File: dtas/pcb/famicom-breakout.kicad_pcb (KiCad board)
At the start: 2 copper layers, 88.5 x 57.4 mm, 23 parts

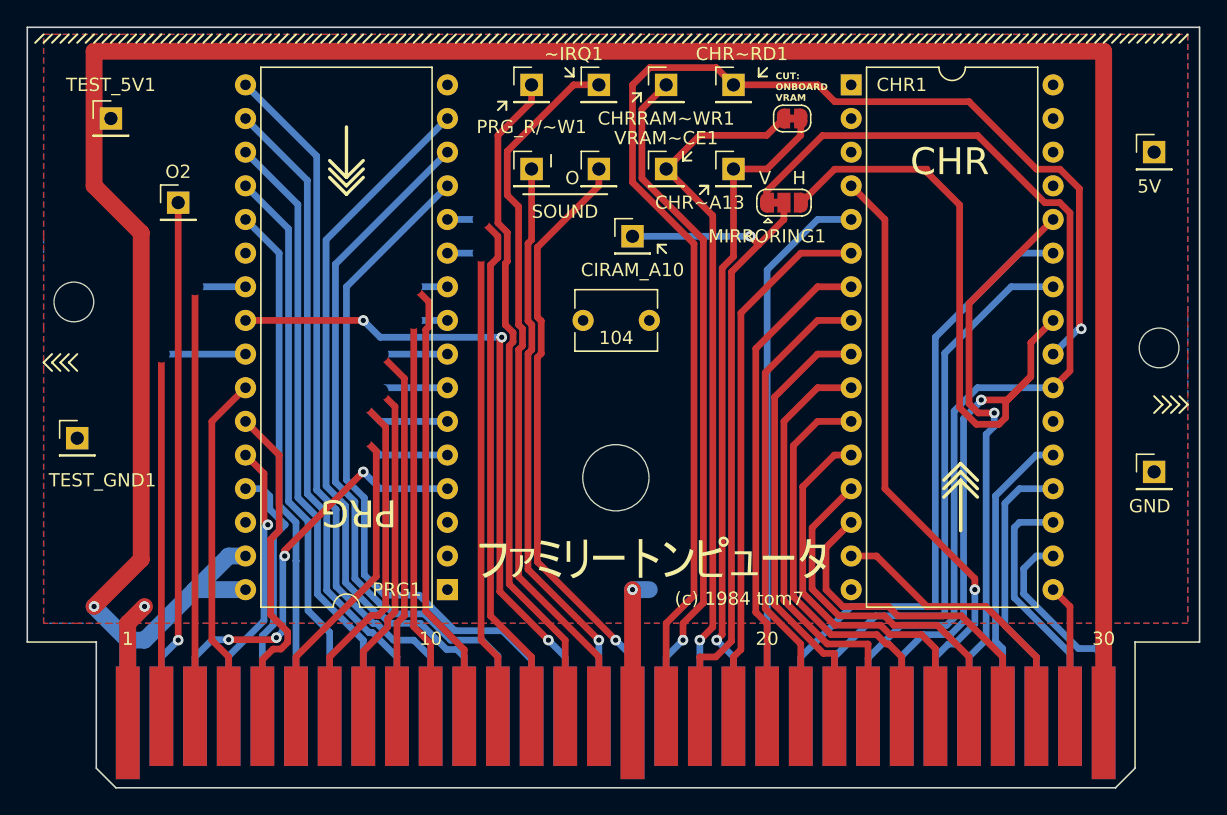
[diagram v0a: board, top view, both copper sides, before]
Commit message: Version 2 of board, which just adds many additional test points and jumpers so I can debug the thing
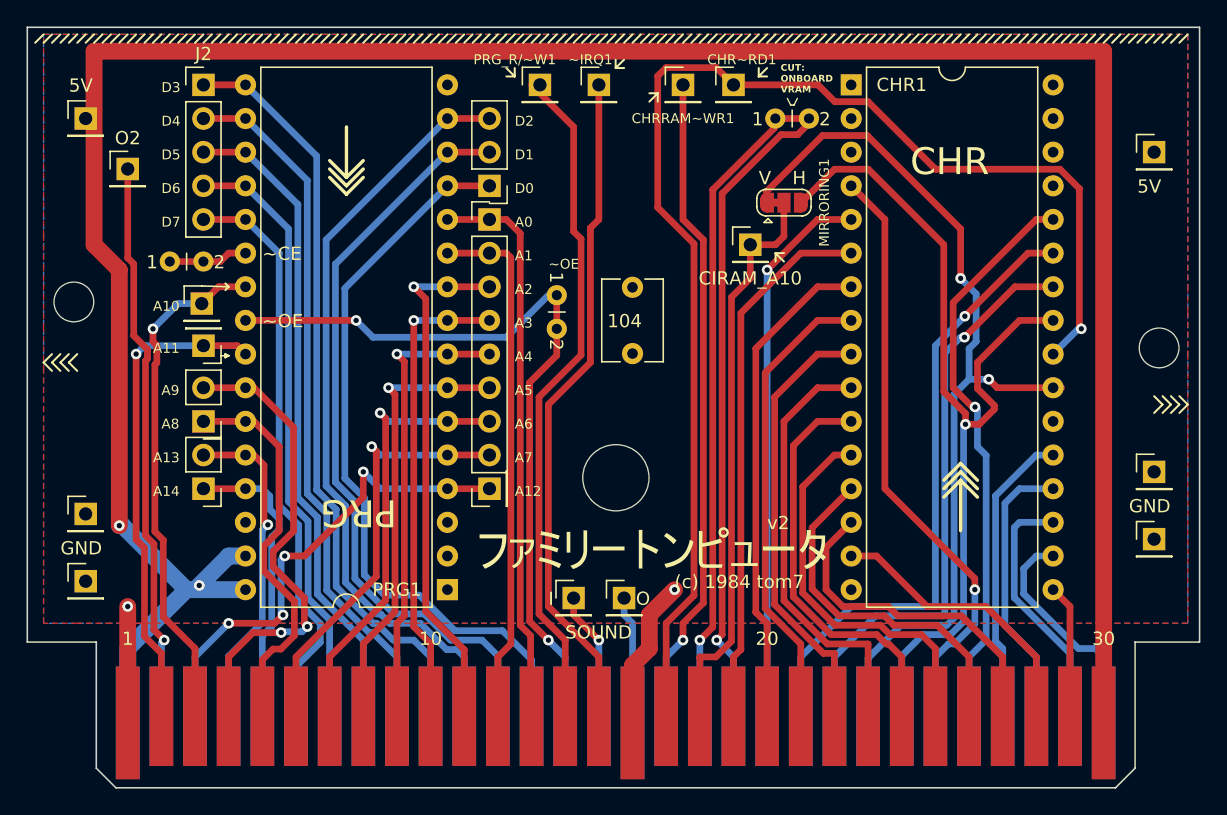
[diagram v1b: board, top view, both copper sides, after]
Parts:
- removed CHR~A13, VRAM~CE1: Conn_01x01, Connector_PinHeader_2.54mm:PinHeader_1x01_P2.54mm_Vertical
- added A10: PRG_ADDR_A10, Connector_PinHeader_2.54mm:PinHeader_1x01_P2.54mm_Vertical, F.Cu at (42.4, 52.1)
- added A11: PRG_ADDR_A11, Connector_PinHeader_2.54mm:PinHeader_1x01_P2.54mm_Vertical, F.Cu at (42.5, 55.2)
- added A12: PRG_ADDR_A12, Connector_PinHeader_2.54mm:PinHeader_1x01_P2.54mm_Vertical, F.Cu at (64.1, 66.0)
- added J1: PRG_DATA0_2, Connector_PinHeader_2.54mm:PinHeader_1x03_P2.54mm_Vertical, F.Cu at (64.1, 43.2)
- added J2: PRG_DATA3_7, Connector_PinHeader_2.54mm:PinHeader_1x05_P2.54mm_Vertical, F.Cu at (42.5, 35.6)
- added J3: PRG_ADDR_0_7, Connector_PinHeader_2.54mm:PinHeader_1x08_P2.54mm_Vertical, F.Cu at (64.1, 45.7)
- added J4: PRG_ADDR_8_9, Connector_PinHeader_2.54mm:PinHeader_1x02_P2.54mm_Vertical, F.Cu at (42.5, 61.0)
- added J5: PRG_ADDR_13_14, Connector_PinHeader_2.54mm:PinHeader_1x02_P2.54mm_Vertical, F.Cu at (42.5, 66.0)
- added JP2: PRG_OE_44, famicom:testjumperclosed, F.Cu at (69.2, 52.7)
- added JP3: PRG_CE_GND, famicom:testjumperclosed, F.Cu at (41.3, 48.9)
- added TEST_GND3: Conn_01x01, Connector_PinHeader_2.54mm:PinHeader_1x01_P2.54mm_Vertical, F.Cu at (33.7, 73.0)
- added TEST_GND4: Conn_01x01, Connector_PinHeader_2.54mm:PinHeader_1x01_P2.54mm_Vertical, F.Cu at (114.3, 69.8)
- JP1: footprint Jumper:SolderJumper-2_P1.3mm_Bridged_RoundedPad1.0x1.5mm -> famicom:testjumperclosed
- moved SOUND_I1 32.5 mm to (70.5, 74.3)
- moved SOUND_O1 32.4 mm to (74.3, 74.3)
- moved CIRAM_A10 8.91 mm to (83.8, 47.6)
- moved TEST_GND1 5.75 mm to (33.7, 67.9)
- moved O2 4.58 mm to (36.8, 41.9)
- moved C1 4.49 mm to (74.9, 55.8), turned to 90 degrees
- moved TEST_5V1 1.91 mm to (33.7, 38.1)
- moved CHRRAM~WR1 1.27 mm to (78.7, 35.6)
- moved PRG_R/~W1 0.63 mm to (67.9, 35.6)
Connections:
- PRG1 pad 22: GND -> Net-(JP3-B)
- PRG1 pad 24: Net-(EDGE1-PRG_ROM_~CE) -> Net-(JP2-A)
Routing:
- net Net-(EDGE1-SOUND_O): track 46.9 -> 9.68 mm, vias 1 -> 0
- net Net-(EDGE1-SOUND_I): track 43.9 -> 9.71 mm
- net Net-(JP2-A): track 0.00 -> 24.7 mm, vias 0 -> 1
- net Net-(EDGE1-PRG_ROM_~CE): track 50.6 -> 31.1 mm, vias 3 -> 1
- net Net-(EDGE1-PRG_A09): track 26.4 -> 36.1 mm, vias 0 -> 2
- net Net-(CIRAM_A10-Pin_1): track 51.9 -> 43.2 mm, vias 1 -> 0
- net Net-(CHR1-A10): track 77.6 -> 70.1 mm, vias 0 -> 2
- net Net-(CHR1-A11): track 74.6 -> 67.4 mm
- net Net-(EDGE1-VRAM_~CE): track 53.6 -> 47.4 mm
- net 5v: track 196.9 -> 191.8 mm, vias 1 -> 2
- net Net-(EDGE1-PRG_D7): track 39.1 -> 43.8 mm
- net Net-(EDGE1-PRG_A08): track 25.2 -> 29.6 mm
- net Net-(EDGE1-~IRQ): track 54.7 -> 50.8 mm
- net Net-(EDGE1-PRG_A13): track 21.6 -> 25.2 mm
- net Net-(A12-Pin_1): track 33.3 -> 36.8 mm
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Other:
- board text added: "A0"
- board text added: "A1"
- board text added: "A10"
- board text added: "A11"
- board text added: "A12"
- board text added: "A13"
- board text added: "A14"
- board text added: "A2"
- board text added: "A3"
- board text added: "A4"
- board text added: "A5"
- board text added: "A6"
- board text added: "A7"
- board text added: "A8"
- board text added: "A9"
- board text added: "D0"
- board text added: "D1"
- board text added: "D2"
- board text added: "D3"
- board text added: "D4"
- board text added: "D5"
- board text added: "D6"
- board text added: "D7"
- board text added: "v2"
- board text added: "~CE"
- board text added: "~OE"
